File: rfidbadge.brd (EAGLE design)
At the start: 93.7 x 48.2 mm, 59 parts, among them Q1 BSS123, U1 ATMEGA328P_TQFP, U2 CLRC663, Y1 27.12 MHz

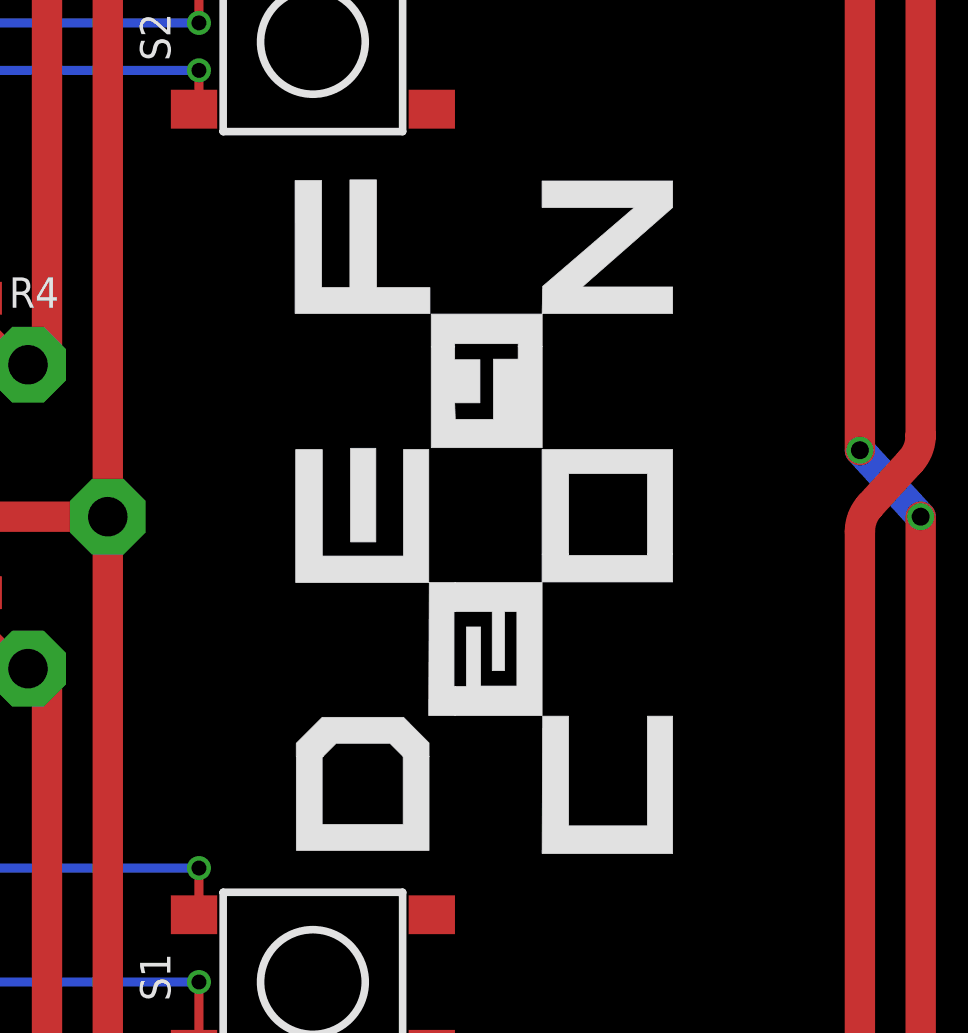
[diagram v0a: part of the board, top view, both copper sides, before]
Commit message: Replace DEF CON 24 logo with BioHack Village logo
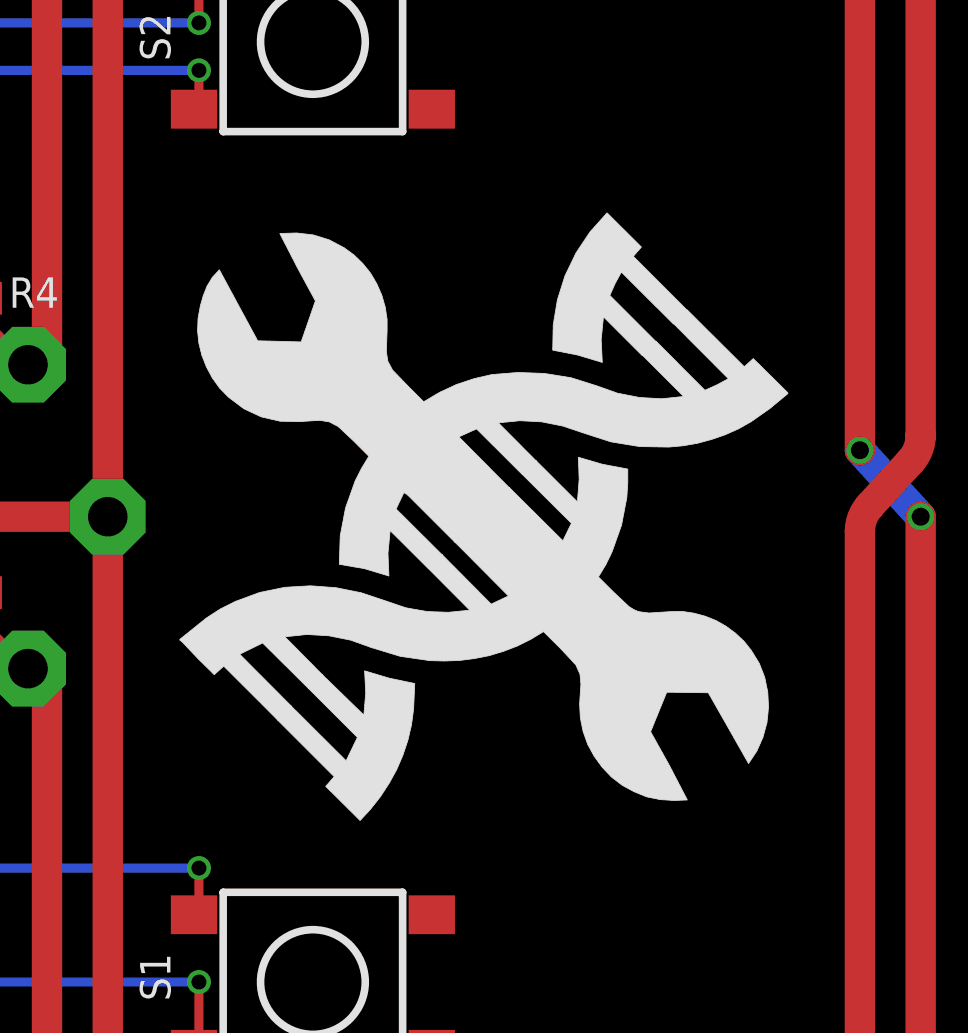
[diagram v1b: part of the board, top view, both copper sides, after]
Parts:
- U$1: value DC24LOGO -> BHVLOGO; device artwork:DC24LOGO -> artwork:BHVLOGO
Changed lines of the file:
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@@
 </class>
 </classes>
-<designrules name="dirt_cheap_dirty_boards.v1">
+<designrules name="dirt_cheap_dirty_boards.v1 *">
 <description language="en">&lt;b&gt;Dirty Cheap Dirty Board Design Rules&lt;/b&gt;
 &lt;br&gt;
@@
 <attribute name="VALUE" x="61.4375" y="9.3825" size="1.778" layer="27" rot="R90"/>
 </element>
-<element name="U$1" library="artwork" package="DC24LOGO" value="DC24LOGO" x="77.47" y="24.13" rot="R90"/>
+<element name="U$1" library="artwork" package="BHVLOGO" value="BHVLOGO" x="77.47" y="24.13" rot="R90"/>
 </elements>
 <signals>
